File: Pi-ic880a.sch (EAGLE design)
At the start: 23 parts, among them U1 IC880A, U2 BR24G32-3, U3 DS3231SN

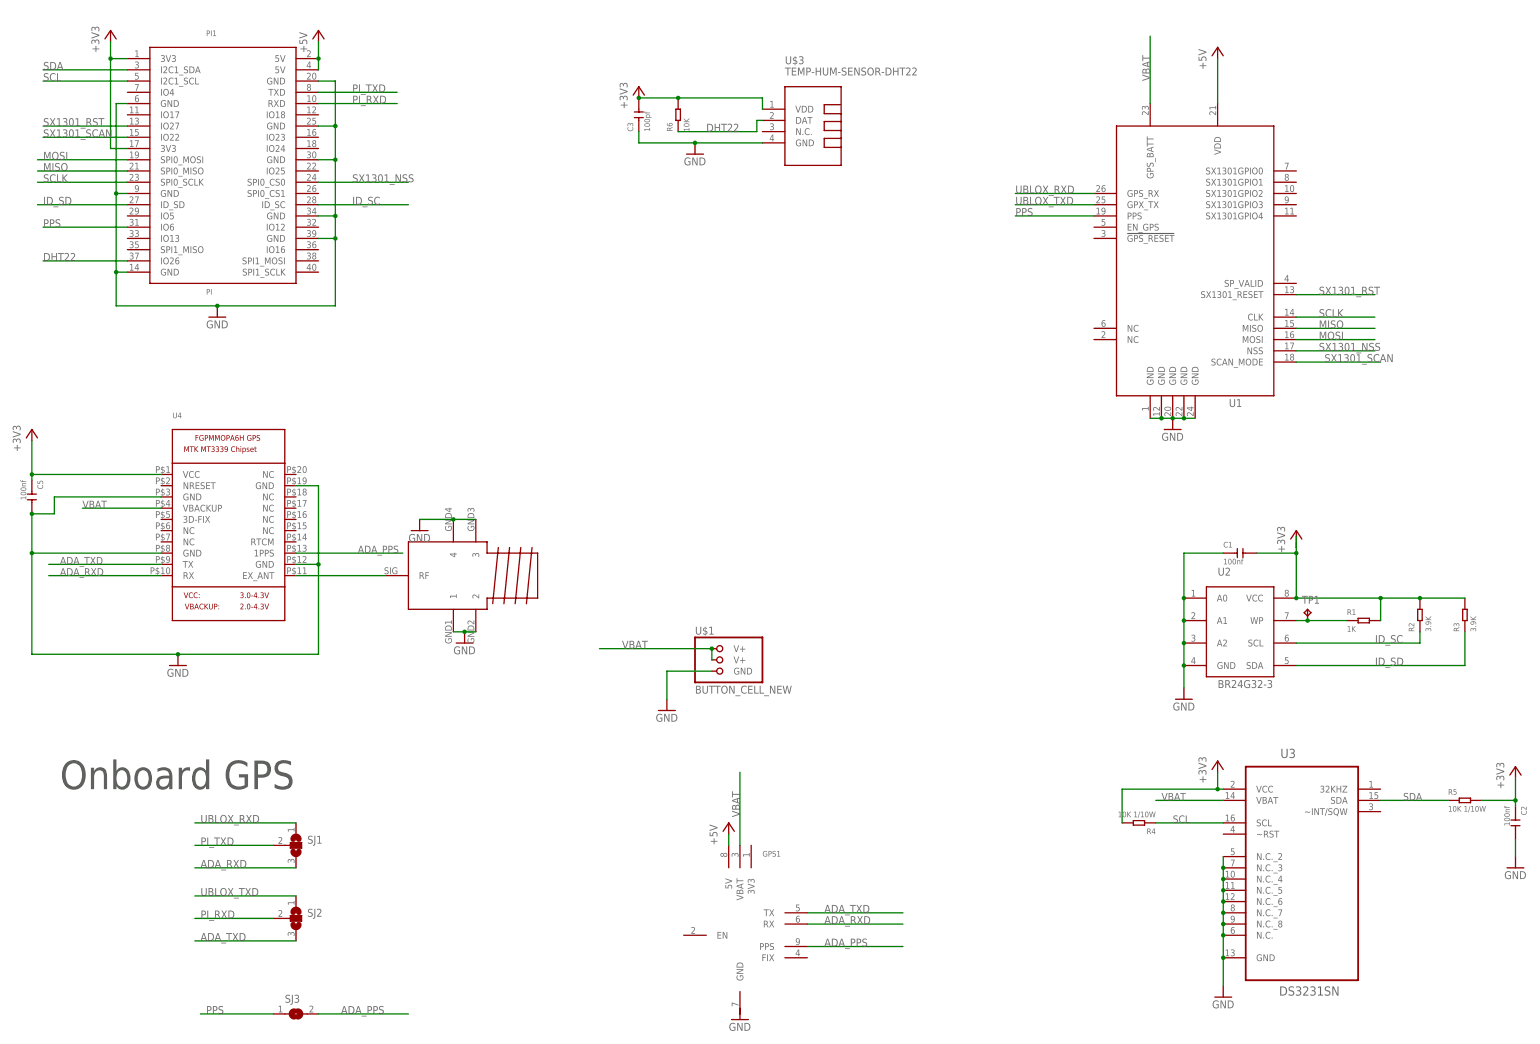
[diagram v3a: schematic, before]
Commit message: Added jumpers for BAT more work on labelling added test pads for VBAT
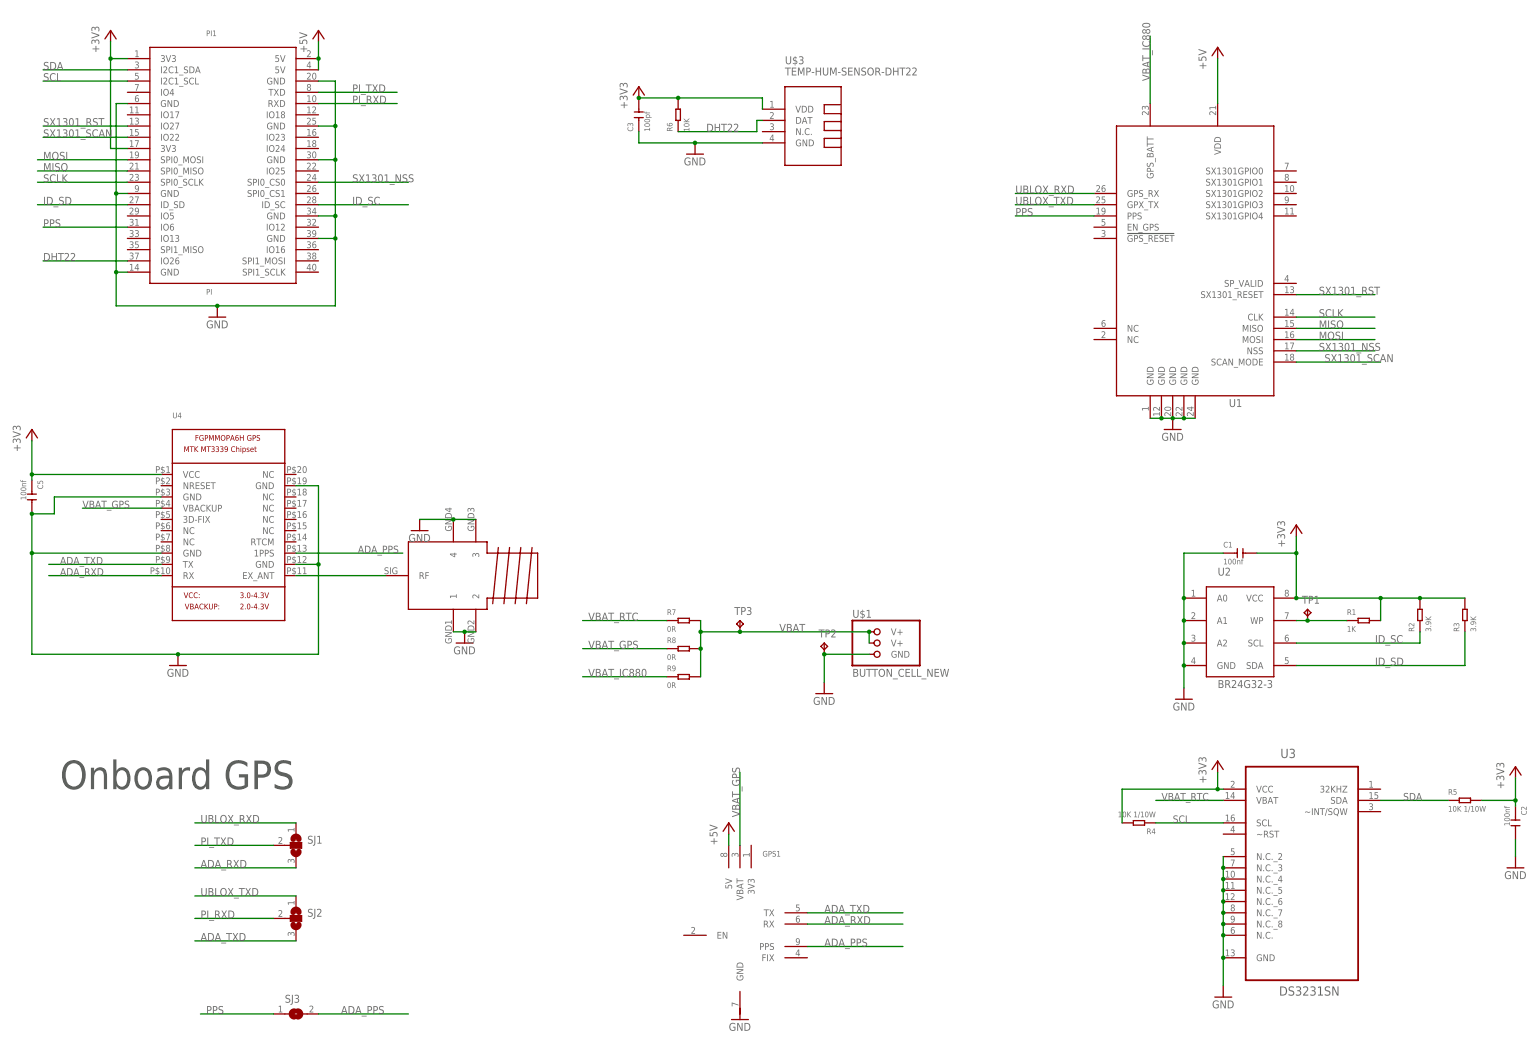
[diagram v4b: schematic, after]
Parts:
- added R7, R8, R9: 0R, Seeed-Resistor:SMD-RES-0R-5%-1/10W(0603)
- added TP2, TP3: TPB2,54, testpad:TPB2,54
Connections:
- new net VBAT_GPS: GPS1.VBAT, R8.1, U4.VBACKUP
- new net VBAT_IC880: R9.1, U1.GPS_BATT
- new net VBAT_RTC: R7.1, U3.VBAT
- net GND: now also TP2.TP
- net VBAT: now also R7.2, R8.2, R9.2, TP3.TP; no longer GPS1.VBAT, U1.GPS_BATT, U3.VBAT, U4.VBACKUP
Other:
- moved on the sheet: U$1
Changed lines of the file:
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@@
 <?xml version="1.0" encoding="utf-8"?>
 <!DOCTYPE eagle SYSTEM "eagle.dtd">
-<eagle version="8.3.2">
+<eagle version="8.4.0">
 <drawing>
 <settings>
@@
 <part name="+3V6" library="supply1" library_urn="urn:adsk.eagle:library:371" deviceset="+3V3" device=""/>
 <part name="GND5" library="supply1" library_urn="urn:adsk.eagle:library:371" deviceset="GND" device=""/>
+<part name="TP2" library="testpad" library_urn="urn:adsk.eagle:library:385" deviceset="TP" device="B2,54" package3d_urn="urn:adsk.eagle:package:27948/1"/>
+<part name="R7" library="Seeed-Resistor" library_urn="urn:adsk.eagle:library:474" deviceset="SMD-RES-0R-5%-1/10W(0603)" device="" package3d_urn="urn:adsk.eagle:package:32791/1" value="0R"/>
+<part name="R8" library="Seeed-Resistor" library_urn="urn:adsk.eagle:library:474" deviceset="SMD-RES-0R-5%-1/10W(0603)" device="" package3d_urn="urn:adsk.eagle:package:32791/1" value="0R"/>
+<part name="R9" library="Seeed-Resistor" library_urn="urn:adsk.eagle:library:474" deviceset="SMD-RES-0R-5%-1/10W(0603)" device="" package3d_urn="urn:adsk.eagle:package:32791/1" value="0R"/>
+<part name="TP3" library="testpad" library_urn="urn:adsk.eagle:library:385" deviceset="TP" device="B2,54" package3d_urn="urn:adsk.eagle:package:27948/1"/>
 </parts>
 <sheets>
@@
 <instance part="R2" gate="G$1" x="347.98" y="120.65" rot="R90"/>
 <instance part="R3" gate="G$1" x="358.14" y="120.65" rot="R90"/>
-<instance part="+3V1" gate="G$1" x="320.04" y="139.7"/>
+<instance part="+3V1" gate="G$1" x="320.04" y="140.97"/>
 <instance part="TP1" gate="G$1" x="322.58" y="121.92"/>
 <instance part="C2" gate="G$1" x="369.57" y="73.66" rot="R270"/>
@@
 <instance part="SJ2" gate="G$1" x="93.98" y="52.07"/>
 <instance part="SJ3" gate="1" x="93.98" y="30.48"/>
-<instance part="U$1" gate="G$1" x="193.04" y="110.49"/>
-<instance part="GND8" gate="1" x="177.8" y="99.06"/>
+<instance part="U$1" gate="G$1" x="228.6" y="114.3"/>
+<instance part="GND8" gate="1" x="213.36" y="102.87"/>
 <instance part="PI1" gate="G$1" x="78.74" y="223.52"/>
 <instance part="GND9" gate="1" x="76.2" y="187.96"/>
@@
 <instance part="+3V6" gate="G$1" x="171.45" y="240.03"/>
 <instance part="GND5" gate="1" x="184.15" y="224.79"/>
+<instance part="TP2" gate="G$1" x="213.36" y="114.3"/>
+<instance part="R7" gate="G$1" x="181.61" y="119.38"/>
+<instance part="R8" gate="G$1" x="181.61" y="113.03"/>
+<instance part="R9" gate="G$1" x="181.61" y="106.68"/>
+<instance part="TP3" gate="G$1" x="194.31" y="119.38"/>
 </instances>
 <busses>
@@
 <net name="VBAT" class="0">
 <segment>
-<pinref part="U1" gate="G$1" pin="GPS_BATT"/>
-<wire x1="287.02" y1="236.22" x2="287.02" y2="251.46" width="0.1524" layer="91"/>
-<label x="287.02" y="241.3" size="1.778" layer="95" rot="R90"/>
-</segment>
-<segment>
-<pinref part="GPS1" gate="G$1" pin="VBAT"/>
-<wire x1="194.31" y1="68.58" x2="194.31" y2="85.09" width="0.1524" layer="91"/>
-<label x="194.31" y="74.93" size="1.778" layer="95" rot="R90"/>
-</segment>
-<segment>
 <pinref part="U$1" gate="G$1" pin="V+@2"/>
 <pinref part="U$1" gate="G$1" pin="V+@1"/>
-<wire x1="187.96" y1="110.49" x2="187.96" y2="113.03" width="0.1524" layer="91"/>
-<wire x1="187.96" y1="113.03" x2="162.56" y2="113.03" width="0.1524" layer="91"/>
-<junction x="187.96" y="113.03"/>
-<label x="167.64" y="113.03" size="1.778" layer="95"/>
-</segment>
-<segment>
-<pinref part="U4" gate="G$1" pin="VBACKUP"/>
-<wire x1="63.5" y1="144.78" x2="45.72" y2="144.78" width="0.1524" layer="91"/>
-<label x="45.72" y="144.78" size="1.6764" layer="95"/>
-</segment>
-<segment>
-<pinref part="U3" gate="A" pin="VBAT"/>
-<wire x1="303.53" y1="78.74" x2="288.29" y2="78.74" width="0.1524" layer="91"/>
-<label x="289.56" y="78.74" size="1.6764" layer="95"/>
+<wire x1="223.52" y1="114.3" x2="223.52" y2="116.84" width="0.1524" layer="91"/>
+<wire x1="223.52" y1="116.84" x2="194.31" y2="116.84" width="0.1524" layer="91"/>
+<junction x="223.52" y="116.84"/>
+<label x="203.2" y="116.84" size="1.778" layer="95"/>
+<pinref part="R7" gate="G$1" pin="2"/>
+<pinref part="R8" gate="G$1" pin="2"/>
+<wire x1="194.31" y1="116.84" x2="185.42" y2="116.84" width="0.1524" layer="91"/>
+<wire x1="185.42" y1="119.38" x2="185.42" y2="116.84" width="0.1524" layer="91"/>
+<pinref part="R9" gate="G$1" pin="2"/>
+<wire x1="185.42" y1="116.84" x2="185.42" y2="113.03" width="0.1524" layer="91"/>
+<wire x1="185.42" y1="113.03" x2="185.42" y2="106.68" width="0.1524" layer="91"/>
+<junction x="185.42" y="113.03"/>
+<junction x="185.42" y="116.84"/>
+<pinref part="TP3" gate="G$1" pin="TP"/>
+<junction x="194.31" y="116.84"/>
 </segment>
 </net>
@@
 <segment>
 <pinref part="U$1" gate="G$1" pin="GND"/>
-<wire x1="187.96" y1="107.95" x2="177.8" y2="107.95" width="0.1524" layer="91"/>
-<wire x1="177.8" y1="107.95" x2="177.8" y2="101.6" width="0.1524" layer="91"/>
+<wire x1="223.52" y1="111.76" x2="213.36" y2="111.76" width="0.1524" layer="91"/>
+<wire x1="213.36" y1="111.76" x2="213.36" y2="105.41" width="0.1524" layer="91"/>
 <pinref part="GND8" gate="1" pin="GND"/>
+<pinref part="TP2" gate="G$1" pin="TP"/>
+<junction x="213.36" y="111.76"/>
 </segment>
 <segment>
@@
 <wire x1="320.04" y1="134.62" x2="320.04" y2="124.46" width="0.1524" layer="91"/>
 <pinref part="+3V1" gate="G$1" pin="+3V3"/>
-<wire x1="320.04" y1="134.62" x2="320.04" y2="135.89" width="0.1524" layer="91"/>
 <junction x="320.04" y="134.62"/>
 <pinref part="R3" gate="G$1" pin="2"/>
 <pinref part="R2" gate="G$1" pin="2"/>
-<wire x1="320.04" y1="135.89" x2="320.04" y2="137.16" width="0.1524" layer="91"/>
+<wire x1="320.04" y1="134.62" x2="320.04" y2="138.43" width="0.1524" layer="91"/>
 <wire x1="358.14" y1="124.46" x2="347.98" y2="124.46" width="0.1524" layer="91"/>
 <wire x1="320.04" y1="124.46" x2="339.09" y2="124.46" width="0.1524" layer="91"/>
@@
 <wire x1="339.09" y1="119.38" x2="339.09" y2="124.46" width="0.1524" layer="91"/>
 <junction x="339.09" y="124.46"/>
-<wire x1="320.04" y1="135.89" x2="320.04" y2="138.43" width="0.1524" layer="91"/>
 </segment>
 <segment>
@@
 </segment>
 </net>
+<net name="VBAT_GPS" class="0">
+<segment>
+<pinref part="GPS1" gate="G$1" pin="VBAT"/>
+<wire x1="194.31" y1="68.58" x2="194.31" y2="85.09" width="0.1524" layer="91"/>
+<label x="194.31" y="74.93" size="1.778" layer="95" rot="R90"/>
+</segment>
+<segment>
+<pinref part="U4" gate="G$1" pin="VBACKUP"/>
+<wire x1="63.5" y1="144.78" x2="45.72" y2="144.78" width="0.1524" layer="91"/>
+<label x="45.72" y="144.78" size="1.6764" layer="95"/>
+</segment>
+<segment>
+<pinref part="R8" gate="G$1" pin="1"/>
+<wire x1="177.8" y1="113.03" x2="158.75" y2="113.03" width="0.1524" layer="91"/>
+<label x="160.02" y="113.03" size="1.778" layer="95"/>
+</segment>
+</net>
+<net name="VBAT_IC880" class="0">
+<segment>
+<pinref part="U1" gate="G$1" pin="GPS_BATT"/>
+<wire x1="287.02" y1="236.22" x2="287.02" y2="251.46" width="0.1524" layer="91"/>
+<label x="287.02" y="241.3" size="1.778" layer="95" rot="R90"/>
+</segment>
+<segment>
+<pinref part="R9" gate="G$1" pin="1"/>
+<wire x1="177.8" y1="106.68" x2="158.75" y2="106.68" width="0.1524" layer="91"/>
+<label x="160.02" y="106.68" size="1.778" layer="95"/>
+</segment>
+</net>
+<net name="VBAT_RTC" class="0">
+<segment>
+<pinref part="U3" gate="A" pin="VBAT"/>
+<wire x1="303.53" y1="78.74" x2="288.29" y2="78.74" width="0.1524" layer="91"/>
+<label x="289.56" y="78.74" size="1.6764" layer="95"/>
+</segment>
+<segment>
+<pinref part="R7" gate="G$1" pin="1"/>
+<wire x1="177.8" y1="119.38" x2="158.75" y2="119.38" width="0.1524" layer="91"/>
+<label x="160.02" y="119.38" size="1.778" layer="95"/>
+</segment>
+</net>
